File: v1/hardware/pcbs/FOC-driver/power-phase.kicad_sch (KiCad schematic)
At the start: 14 parts, among them Q1 BSC093N15NS5, Q2 BSC093N15NS5

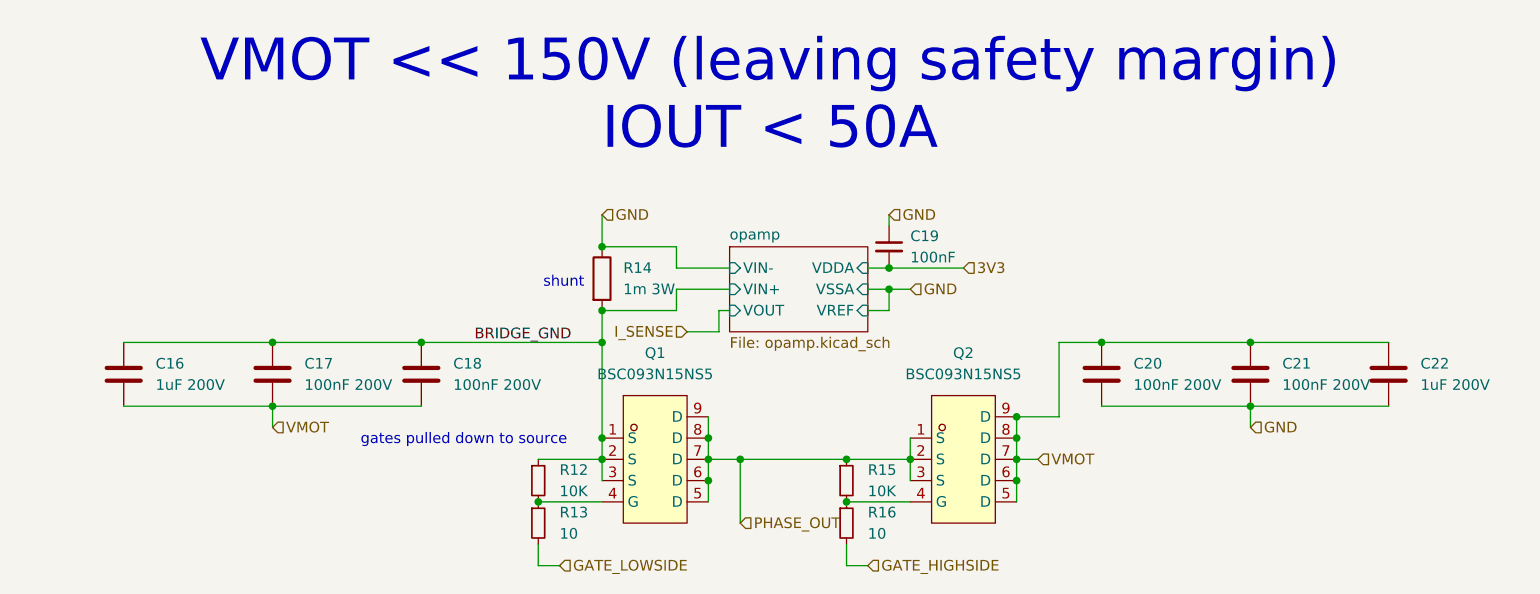
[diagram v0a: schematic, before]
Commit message: new FOC driver schematic
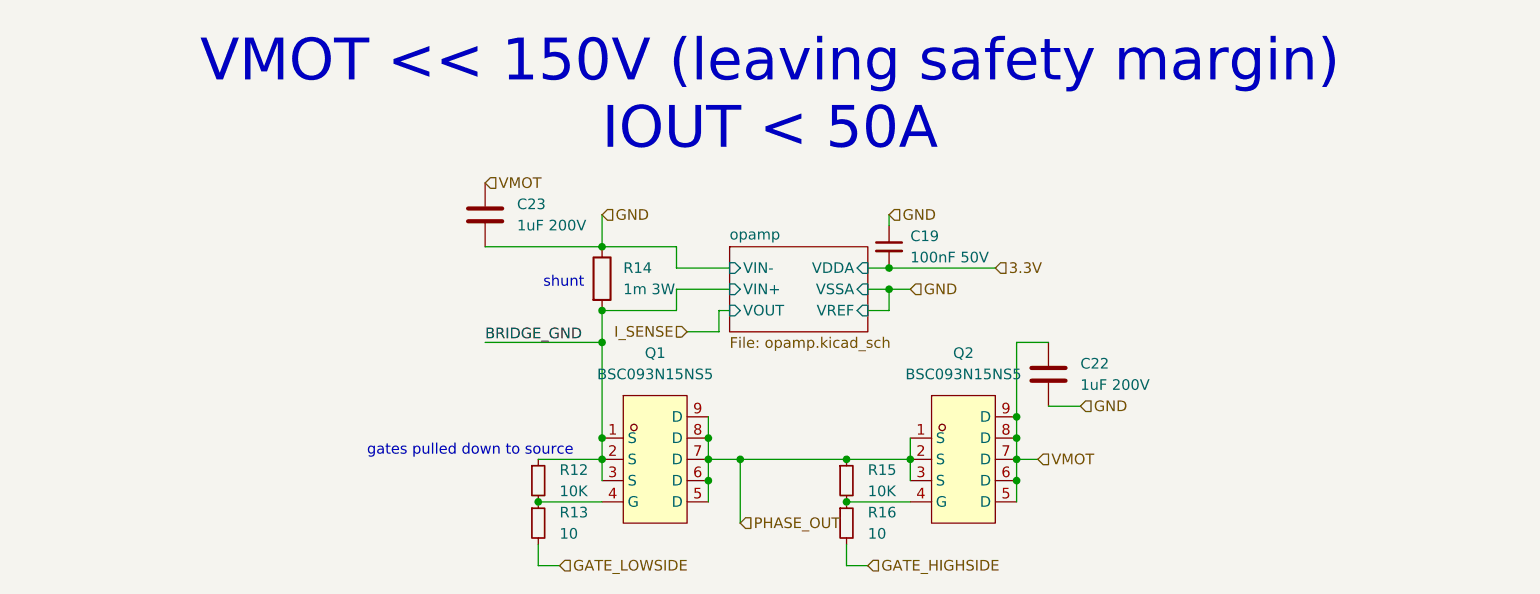
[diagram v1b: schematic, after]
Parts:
- removed C16: 1uF 200V, Capacitor_SMD:C_1812_4532Metric, symbol symbols:C
- removed C17, C18, C20, C21: 100nF 200V, Capacitor_SMD:C_0805_2012Metric, symbol symbols:C
- added C23: 1uF 200V, Capacitor_SMD:C_1812_4532Metric, symbol symbols:C
- C19: value 100nF -> 100nF 50V; footprint Capacitor_SMD:C_0603_1608Metric -> Capacitor_SMD:C_0402_1005Metric
- R12, R13: footprint Resistor_SMD:R_0603_1608Metric -> Resistor_SMD:R_0402_1005Metric
- R15, R16: footprint Resistor_SMD:R_0805_2012Metric -> Resistor_SMD:R_0402_1005Metric
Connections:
- net GND: now also C23.2
- net VMOT: now also C23.1
- net 3V3 renamed 3.3V
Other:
- moved on the sheet: C22
